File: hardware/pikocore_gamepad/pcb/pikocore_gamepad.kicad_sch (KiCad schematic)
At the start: 59 parts, among them J1 PHONES, J4 ST7789_240x240, J5 SPEAKER 8R, SW10 BTN_R, SW11 BTN_START, SW12 BTN_SELECT, SW13 NAV5, SW15 PWR, SW5 BTN_X, SW6 BTN_Y, SW7 BTN_A, SW8 BTN_B, SW9 BTN_L, U1 RP2350-Plus-16MB, U2 TPS61023DRLR, U3 NJM4556AD, U4 PAM8302A, U5 PCM5102APWR

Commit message: hw: snapshot del pipeline de pikocore_gamepad — punto de rollback
Commit de resguardo, no un cambio con una idea sola. Junta todo el trabajo del
pipeline de PCB que estaba sin commitear, para que exista un estado al que
volver antes de correr el ciclo de ruteo completo, que reescribe el
esquematico, las 5 hojas, el netlist y la placa, y cuyo autorouter no es
determinista.

Sin esto, un `git checkout` despues de un re-ruteo fallido devolvia el
esquematico PLANO de hace dias, no el jerarquico de ahora.

Lo mas importante que entra: tres scripts que el ciclo NECESITA y que estaban
sin trackear —

  plane_vias.py    vias que conectan pads SMD de GND/3V3 a los planos internos
  manual_tracks.py pistas trazadas a mano que entran al DSN como preexistentes
  gen_fab.py       paquete de fabricacion para JLCPCB, con G-0 como puerta

Los dos primeros van ANTES del export al DSN, no despues; el motivo y lo que
costo descubrirlo estan documentados en la checklist.

Y el esquematico partido en 5 hojas jerarquicas, que vivia solo en el working
tree: el root perdio 2993 lineas porque el contenido se mudo a
01_alimentacion, 02_mcu_controles, 03_dac, 04_opamp y 05_salidas, ninguna de
las cuales estaba trackeada. gen_sch.py las genera desde HOJAS.

Estado verificado al momento del commit, corriendo las puertas de verdad:

  201 tests                             OK
  checks/run_all.py (G-0/G-5/G-4/G-2/P) todas pasan
  ERC                                   0 errores, 2 avisos
  DRC                                   2 errores, 7 avisos
  unconnected_items                     0

Los 2 errores de DRC son conocidos y quedan abiertos a proposito: vias de GND
y 3V3 encimadas sobre pads adyacentes de U5 (TSSOP-20, paso 0.65mm), porque
plane_vias.py dimensiona cada via mirando solo pads y no las vias que el mismo
ya coloco. Arreglarlo obliga al ciclo completo, que es justamente lo que este
commit viene a proteger.

Queda fuera a proposito: freerouting-1.9.0.jar (la checklist dice que no se
vers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
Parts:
- removed C10, C11, C13, C15, C20, C27, C7: 100nF, Capacitor_SMD:C_0603_1608Metric, symbol pikocore_gamepad:C
- removed C12, C14, C16, C28: 10uF, Capacitor_SMD:CP_Elec_6.3x5.4, symbol pikocore_gamepad:CP
- removed C17, C18: 2n2, Capacitor_SMD:C_0603_1608Metric, symbol pikocore_gamepad:C
- removed C19, C6: 100uF, Capacitor_SMD:CP_Elec_6.3x5.4, symbol pikocore_gamepad:CP
- removed C21, C22, C25, C26: 1uF, Capacitor_SMD:C_0603_1608Metric, symbol pikocore_gamepad:C
- removed C23, C24: 470uF, Capacitor_SMD:CP_Elec_6.3x5.4, symbol pikocore_gamepad:CP
- removed C4: 10uF, Capacitor_SMD:C_0603_1608Metric, symbol pikocore_gamepad:C
- removed C5: 22uF, Capacitor_SMD:C_0603_1608Metric, symbol pikocore_gamepad:C
- removed C8, C9: 2u2, Capacitor_SMD:C_0603_1608Metric, symbol pikocore_gamepad:C
- removed J1: PHONES, Connector_PinHeader_2.54mm:PinHeader_1x04_P2.54mm_Vertical, symbol pikocore_gamepad:JACK_AUDIO
- removed J4: ST7789_240x240, gamesetup_fp:LCD_ST7789_240x240_7P, symbol pikocore_gamepad:LCD_ST7789
- removed J5: SPEAKER 8R, Connector_JST:JST_PH_B2B-PH-K_1x02_P2.00mm_Vertical, symbol pikocore_gamepad:Conn_01x02
- removed L1, L2: 2u2, Inductor_SMD:L_1210_3225Metric, symbol pikocore_gamepad:L
- removed R10, R12, R14, R15, R16, R17, R9: 10k, Resistor_SMD:R_0603_1608Metric, symbol pikocore_gamepad:R
- removed R11, R13: 20k, Resistor_SMD:R_0603_1608Metric, symbol pikocore_gamepad:R
- removed R4: 1M, Resistor_SMD:R_0603_1608Metric, symbol pikocore_gamepad:R
- removed R5: 200k, Resistor_SMD:R_0603_1608Metric, symbol pikocore_gamepad:R
- removed R6: 100k, Resistor_SMD:R_0603_1608Metric, symbol pikocore_gamepad:R
- removed R7, R8: 470R, Resistor_SMD:R_0603_1608Metric, symbol pikocore_gamepad:R
- removed SW10: BTN_R, Button_Switch_THT:SW_Tactile_SPST_Angled_PTS645Vx39-2LFS, symbol pikocore_gamepad:SW_Push_RA
- removed SW11: BTN_START, gamesetup_lcsc:SW-TH_4P-L4.5-W4.5-P3.00-LS5.5, symbol pikocore_gamepad:SW_Push
- removed SW12: BTN_SELECT, gamesetup_lcsc:SW-TH_4P-L4.5-W4.5-P3.00-LS5.5, symbol pikocore_gamepad:SW_Push
- removed SW13: NAV5, gamesetup_lcsc:SW-TH_WS-1004-ARL10026, symbol pikocore_gamepad:NAV_WS1004
- removed SW15: PWR, gamesetup_lcsc:SW-TH_SK12D07VG3, symbol pikocore_gamepad:SK12D07
- removed SW5: BTN_X, gamesetup_lcsc:SW-TH_4P-L4.5-W4.5-P3.00-LS5.5, symbol pikocore_gamepad:SW_Push
- removed SW6: BTN_Y, gamesetup_lcsc:SW-TH_4P-L4.5-W4.5-P3.00-LS5.5, symbol pikocore_gamepad:SW_Push
- removed SW7: BTN_A, gamesetup_lcsc:SW-TH_4P-L4.5-W4.5-P3.00-LS5.5, symbol pikocore_gamepad:SW_Push
- removed SW8: BTN_B, gamesetup_lcsc:SW-TH_4P-L4.5-W4.5-P3.00-LS5.5, symbol pikocore_gamepad:SW_Push
- removed SW9: BTN_L, Button_Switch_THT:SW_Tactile_SPST_Angled_PTS645Vx39-2LFS, symbol pikocore_gamepad:SW_Push_RA
- removed U1: RP2350-Plus-16MB, gamesetup_fp:RP2350-Plus_Socket, symbol pikocore_gamepad:RP2350-Plus
- removed U2: TPS61023DRLR, Package_TO_SOT_SMD:SOT-563, symbol pikocore_gamepad:TPS61023
- removed U3: NJM4556AD, Package_SO:SOIC-8_3.9x4.9mm_P1.27mm, symbol pikocore_gamepad:NJM4556AD
- removed U4: PAM8302A, gamesetup_lcsc:MSOP-8_L3.0-W3.0-P0.65-LS5.0-BL, symbol pikocore_gamepad:PAM8302A
- removed U5: PCM5102APWR, gamesetup_lcsc:TSSOP-20_L6.5-W4.4-P0.65-LS6.4-BL, symbol pikocore_gamepad:PCM5102A
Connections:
- no-connect marks 17 -> 0
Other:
- added sheet Alimentacion - boost 5V y encendido (01_alimentacion.kicad_sch)
- added sheet Audio analogico - buffer y masa virtual (04_opamp.kicad_sch)
- added sheet Audio digital - DAC PCM5102A (03_dac.kicad_sch)
- added sheet MCU, pantalla y controles (02_mcu_controles.kicad_sch)
- added sheet Salidas - jack, deteccion y parlante (05_salidas.kicad_sch)
- note added: "10 componentes"
- note added: "11 componentes"
- note added: "13 componentes"
- note added: "14 componentes"
- note added: "15 componentes"
- note added: "pikocore_gamepad - PCB de 4 capas (F.Cu / GND / PWR / B.Cu), 120x80mm, panel unico. MCU: modulo Waveshare RP2350-Plus 16MB sobre socket 2x20. La bateria LiPo va al PH1.25 DEL PROPIO MODULO, que trae cargador ETA6096 a bordo: esta placa NO lleva circuito de carga. SW15 no corta la bateria, corta 3V3_EN del modulo, que tiene pull-up interno de 100K a VSYS. TODAS las conexiones son por GLOBAL LABEL,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"
- note removed: "AUDIO: DAC PCM5102A (U5) chip-down, I2S por PIO. SCK (pin 12) a GND = PLL interno desde BCK, no hace falta MCLK. FMT/FLT/DEMP a GND. XSMT con pulldown de 100k: el DAC arranca MUTEADO y el firmware lo libera (anti-pop). La salida del DAC esta centrada en MASA (charge pump, +-2.8V / 2.0 Vrms), por eso el buffer U3 es INVERSOR con ganancia 0.5 y entrada acoplada: 2.0 Vrms no entran en un riel de 5V 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"
- note removed: "ENTRADA: los 12 botones van directo a GPIO del modulo (sin expansor I2C) — ver pinmap.py para la asignacion."
- note removed: "VERIFICAR ANTES DE FABRICAR (correr checks/check_verified.py): - Cotas del modulo LCD que el drawing no acota: vertical de la fila de pines, y el offset de los agujeros (la cota dice 2.19 y la nota china 2.5). - Pinout de TPS61023 y del jack de audio: ninguno viene verificado de V1 y sus simbolos lo dicen. - Valores del lazo del boost (inductor y divisor de realimentacion). Los pinouts de PCM5102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"
- note removed: "pikocore_gamepad - PCB panel unico, 4 capas. MCU Waveshare RP2350-Plus 16MB en socket 2x20. La bateria LiPo va al PH1.25 del propio modulo (cargador ETA6096 a bordo): la placa no lleva circuito de carga. SW15 apaga el rail 3V3 del modulo via 3V3_EN, que tiene pull-up interno de 100K a VSYS."
- title: pikocore_gamepad - panel principal -> pikocore_gamepad - indice

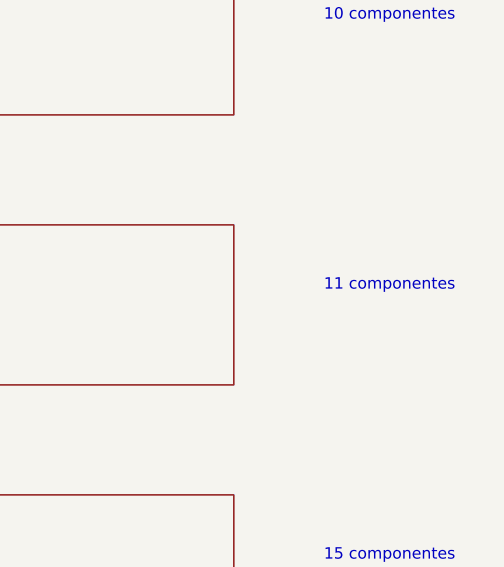
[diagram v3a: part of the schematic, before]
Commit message: hw: D-pad de cuatro tacts 6x6 en lugar del NAV5, re-ruteo determinista del boost
El NAV5 de 5 vias es un solo actuador y no deja pulsar dos direcciones a la
vez, que es lo que piden Up+Down+B+A (reset de FX) y Down+Left+X+B (clock
lock). Vuelven SW1-SW4 (SW_PUSH_6mm) en cruz de 12.5mm centrada en X=30,
espejo del rombo; BTN_OK desaparece y GP26 queda libre con GP27/28; Start
pasa a x=26.75 para centrar su cuerpo en X=30. manual_tracks.py toma la lista
de tacts de netlist.TACTS, sin tercera copia. Tests, stub de firmware y doc
de pinout actualizados (196 tests).

Ruteo: freerouting 2.4.1 se lanza con -Djava.awt.headless=true -mt 1. Con
ventana, un NullPointerException en el repintado de AWT interrumpe el fanout
y el .ses sale con 60+ nets abiertas y exit 0. Las pistas manuales solo a
0/45/90 grados: con otro angulo la normalizacion oscila y aborta. Todo el
lazo del boost va ahora a mano y relativo a U2 (U2_5V hasta C5.1, C7_5V,
L1_VSYS_F, C4_VSYS_F): freerouting cerraba esos tramos una corrida si y
otra no. NPTH_KEEPOUT sube de 0.60 a 0.75 (BTN_R quedaba a 0.36mm del
anclaje de SW10).

Puertas: G-0/G-5/G-4/G-2/placement OK, ERC 0 errores (3 avisos GP26/27/28
reservados), DRC 0 errores / 0 abiertas / 0 paridad, G-F al dia, fab con las
4 capas (38 lineas de BOM, 17 sin LCSC: THT manuales y los 470uF).

Co-Authored-By: Claude Fable 5.1 <noreply@anthropic.com>
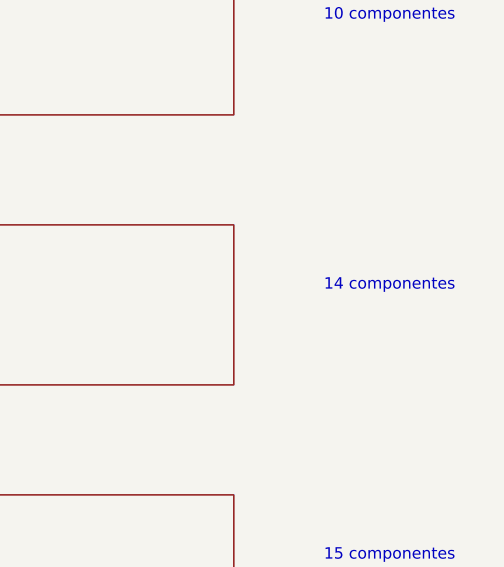
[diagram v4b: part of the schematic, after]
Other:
- note removed: "11 componentes"
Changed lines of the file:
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@@
     )
   )
-  (text "11 componentes" (exclude_from_sim no) (at 205 61 0)
+  (text "14 componentes" (exclude_from_sim no) (at 205 61 0)
     (effects (font (size 1.27 1.27)) (justify left top))
   )

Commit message: hw: pantalla por flex (DM-TFT13-377 24P + FPC 0.5mm) y layout del estudio ergonomico
El modulo LCD de 7 pines pasantes se reemplaza por el panel desnudo
DisplayModule DM-TFT13-377 variante 24 pines (LH133T-IF05, ST7789VW,
datasheet en hardware/pikocore_gamepad/datasheets/) pegado al frente, con
el FPC de 0.5mm al conector J4 XUNPU FPC-05FB-24PH20 (LCSC C2856831, huella
y STEP importados con easyeda2kicad). LCSC no tiene paneles de 1.3" en
stock y la variante de 12 pines usa FPC de 0.7mm, paso para el que LCSC no
vende conector. 4-SPI con IM=1, CS a masa (siempre seleccionado, como el
modulo), RD y DB0-7 a masa, TE a GP26 (LCD_TE). Backlight desde VSYS por
R21 (24R, perilla de brillo) y Q1 2N7002 (C8545) con R22 de pulldown;
C30/C31 de desacoplo. LCD1 es una huella sin pads generada por gen_fp.py
(origen = centro del area activa), DNP para el CPL pero en el BOM.

Layout segun el estudio ergonomico: panel con el BL a 3.0mm del borde
superior (area activa y 4.6-28), D-pad y rombo centrados en y 53.2 con paso
12.5, Select (50, 51) y Start (50, 63) apilados en la columna central, J4 en
(50, 44.6) rot 180 justo donde caen los contactos del flex desplegado,
R19/R20 bajados a y 72.5/75.5 por los pines de B. Los pulgares quedan 8mm
por debajo del vidrio; Up/X al costado de la franja sin vidrio.

G-0 queda ROJO a proposito: LCD_FPC_PIN_ORDER (V-8) no sale del datasheet
(lado de los contactos del FPC); se mide con el panel en mano y, si esta
espejado, J4 va a rot 0. gen_fab.py solo genera con --force hasta entonces.

Pipeline: plane_vias.py saltea el pad si hay una via propia a <0.6mm (los
13 GND del conector a 0.5mm daban hole_to_hole) y el fanout rechaza
candidatos pegados a una via de la misma net; finish_pcb.py borra stubs
colgantes. Tests reescritos para el panel (181). Puertas: G-5/G-4/G-2/
placement OK, 245 conexiones identicas, ERC 0 errores (2 avisos GP27/28),
DRC 0 errores / 0 abiertas / 0 paridad (10 avisos conocidos).

Co-Authored-By: Claude Fable 5.1 <noreply@anth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
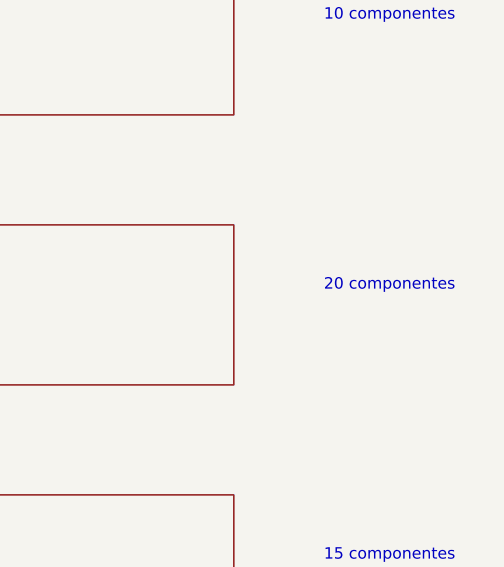
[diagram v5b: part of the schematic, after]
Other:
- note added: "20 componentes"
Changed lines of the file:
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@@
     )
   )
-  (text "14 componentes" (exclude_from_sim no) (at 205 61 0)
+  (text "20 componentes" (exclude_from_sim no) (at 205 61 0)
     (effects (font (size 1.27 1.27)) (justify left top))
   )

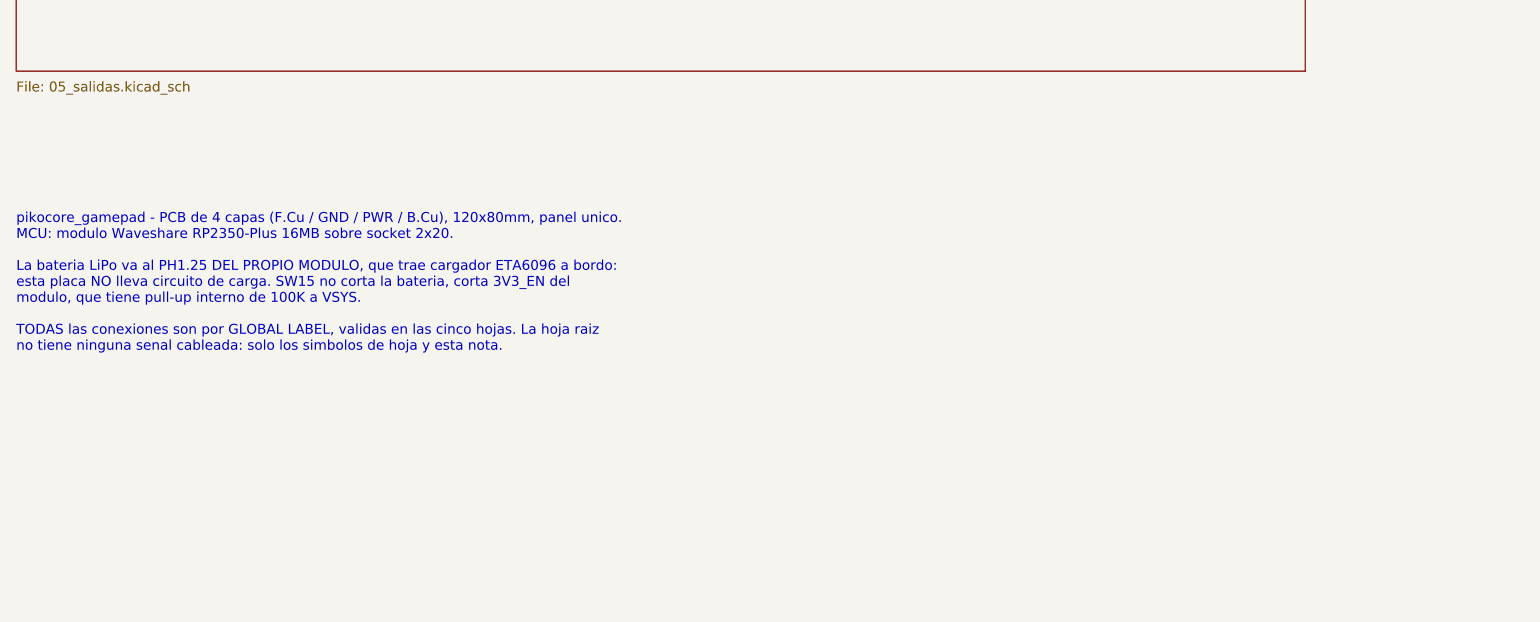
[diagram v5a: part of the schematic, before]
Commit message: hw: MIDI IN/OUT en TRS tipo A (hoja 07_midi, pinouts verificados)
Portado de hw/chipdown-rp2350: J6/J7 (TRS tipo A), U9 74LVC1G17, U10
H11L1SR2M, D3 1N4148W, R40-R43, C56, con la polaridad corregida (Ring ->
220R -> anodo del opto). TestMidi (9 tests), esquematico regenerado en seis
hojas y datasheets de TI SCES351Y y onsemi H11L1M rev 1.0.7.

Co-Authored-By: Claude Sonnet 5.5 <noreply@anthropic.com>
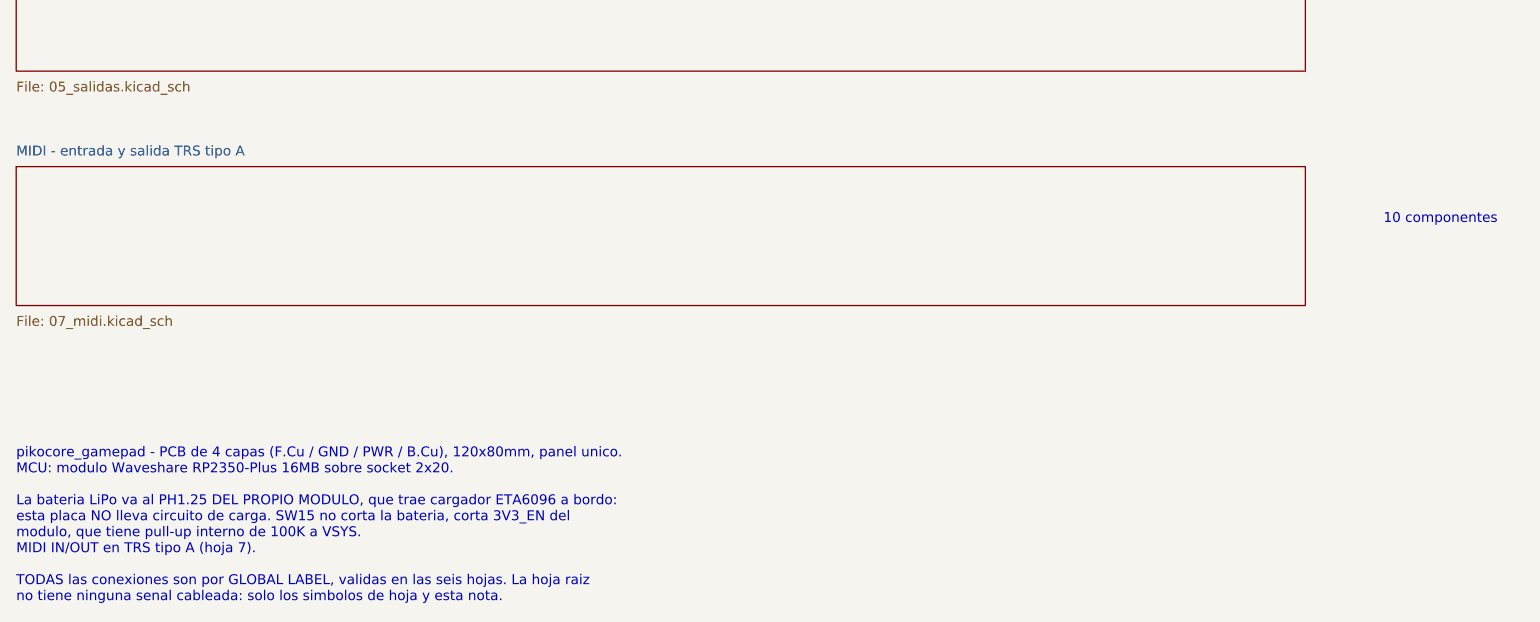
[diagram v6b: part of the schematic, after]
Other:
- added sheet MIDI - entrada y salida TRS tipo A (07_midi.kicad_sch)
- note added: "pikocore_gamepad - PCB de 4 capas (F.Cu / GND / PWR / B.Cu), 120x80mm, panel unico. MCU: modulo Waveshare RP2350-Plus 16MB sobre socket 2x20. La bateria LiPo va al PH1.25 DEL PROPIO MODULO, que trae cargador ETA6096 a bordo: esta placa NO lleva circuito de carga. SW15 no corta la bateria, corta 3V3_EN del modulo, que tiene pull-up interno de 100K a VSYS. MIDI IN/OUT en TRS tipo A (hoja 7). TODAS 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"
- note removed: "pikocore_gamepad - PCB de 4 capas (F.Cu / GND / PWR / B.Cu), 120x80mm, panel unico. MCU: modulo Waveshare RP2350-Plus 16MB sobre socket 2x20. La bateria LiPo va al PH1.25 DEL PROPIO MODULO, que trae cargador ETA6096 a bordo: esta placa NO lleva circuito de carga. SW15 no corta la bateria, corta 3V3_EN del modulo, que tiene pull-up interno de 100K a VSYS. TODAS las conexiones son por GLOBAL LABEL,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"
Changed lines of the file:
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@@
     (effects (font (size 1.27 1.27)) (justify left top))
   )
-  (text "pikocore_gamepad - PCB de 4 capas (F.Cu / GND / PWR / B.Cu), 120x80mm, panel unico.\nMCU: modulo Waveshare RP2350-Plus 16MB sobre socket 2x20.\n\nLa bateria LiPo va al PH1.25 DEL PROPIO MODULO, que trae cargador ETA6096 a bordo:\nesta placa NO lleva circuito de carga. SW15 no corta la bateria, corta 3V3_EN del\nmodulo, que tiene pull-up interno de 100K a VSYS.\n\nTODAS las conexiones son por GLOBAL LABEL, validas en las cinco hojas. La hoja raiz\nno tiene ninguna senal cableada: solo los simbolos de hoja y esta nota." (exclude_from_sim no) (at 30 181 0)
+  (sheet (at 30 175) (size 165 17.78)
+    (stroke (width 0.1524) (type solid))
+    (fill (color 0 0 0 0.0))
+    (property "Sheetname" "MIDI - entrada y salida TRS tipo A" (at 30 173.73 0)
+      (effects (font (size 1.27 1.27)) (justify left bottom))
+    )
+    (property "Sheetfile" "07_midi.kicad_sch" (at 30 194.05 0)
+      (effects (font (size 1.27 1.27)) (justify left top))
+    )
+    (instances
+      (project "pikocore_gamepad"
+        (path "/b1e7c2a4-9f31-4d6e-8a52-3c0f7d418e6b" (page "7"))
+      )
+    )
+  )
+  (text "10 componentes" (exclude_from_sim no) (at 205 181 0)
     (effects (font (size 1.27 1.27)) (justify left top))
   )
+  (text "pikocore_gamepad - PCB de 4 capas (F.Cu / GND / PWR / B.Cu), 120x80mm, panel unico.\nMCU: modulo Waveshare RP2350-Plus 16MB sobre socket 2x20.\n\nLa bateria LiPo va al PH1.25 DEL PROPIO MODULO, que trae cargador ETA6096 a bordo:\nesta placa NO lleva circuito de carga. SW15 no corta la bateria, corta 3V3_EN del\nmodulo, que tiene pull-up interno de 100K a VSYS.\nMIDI IN/OUT en TRS tipo A (hoja 7).\n\nTODAS las conexiones son por GLOBAL LABEL, validas en las seis hojas. La hoja raiz\nno tiene ninguna senal cableada: solo los simbolos de hoja y esta nota." (exclude_from_sim no) (at 30 211 0)
+    (effects (font (size 1.27 1.27)) (justify left top))
+  )
